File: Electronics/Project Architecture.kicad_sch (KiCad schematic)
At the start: 5 parts

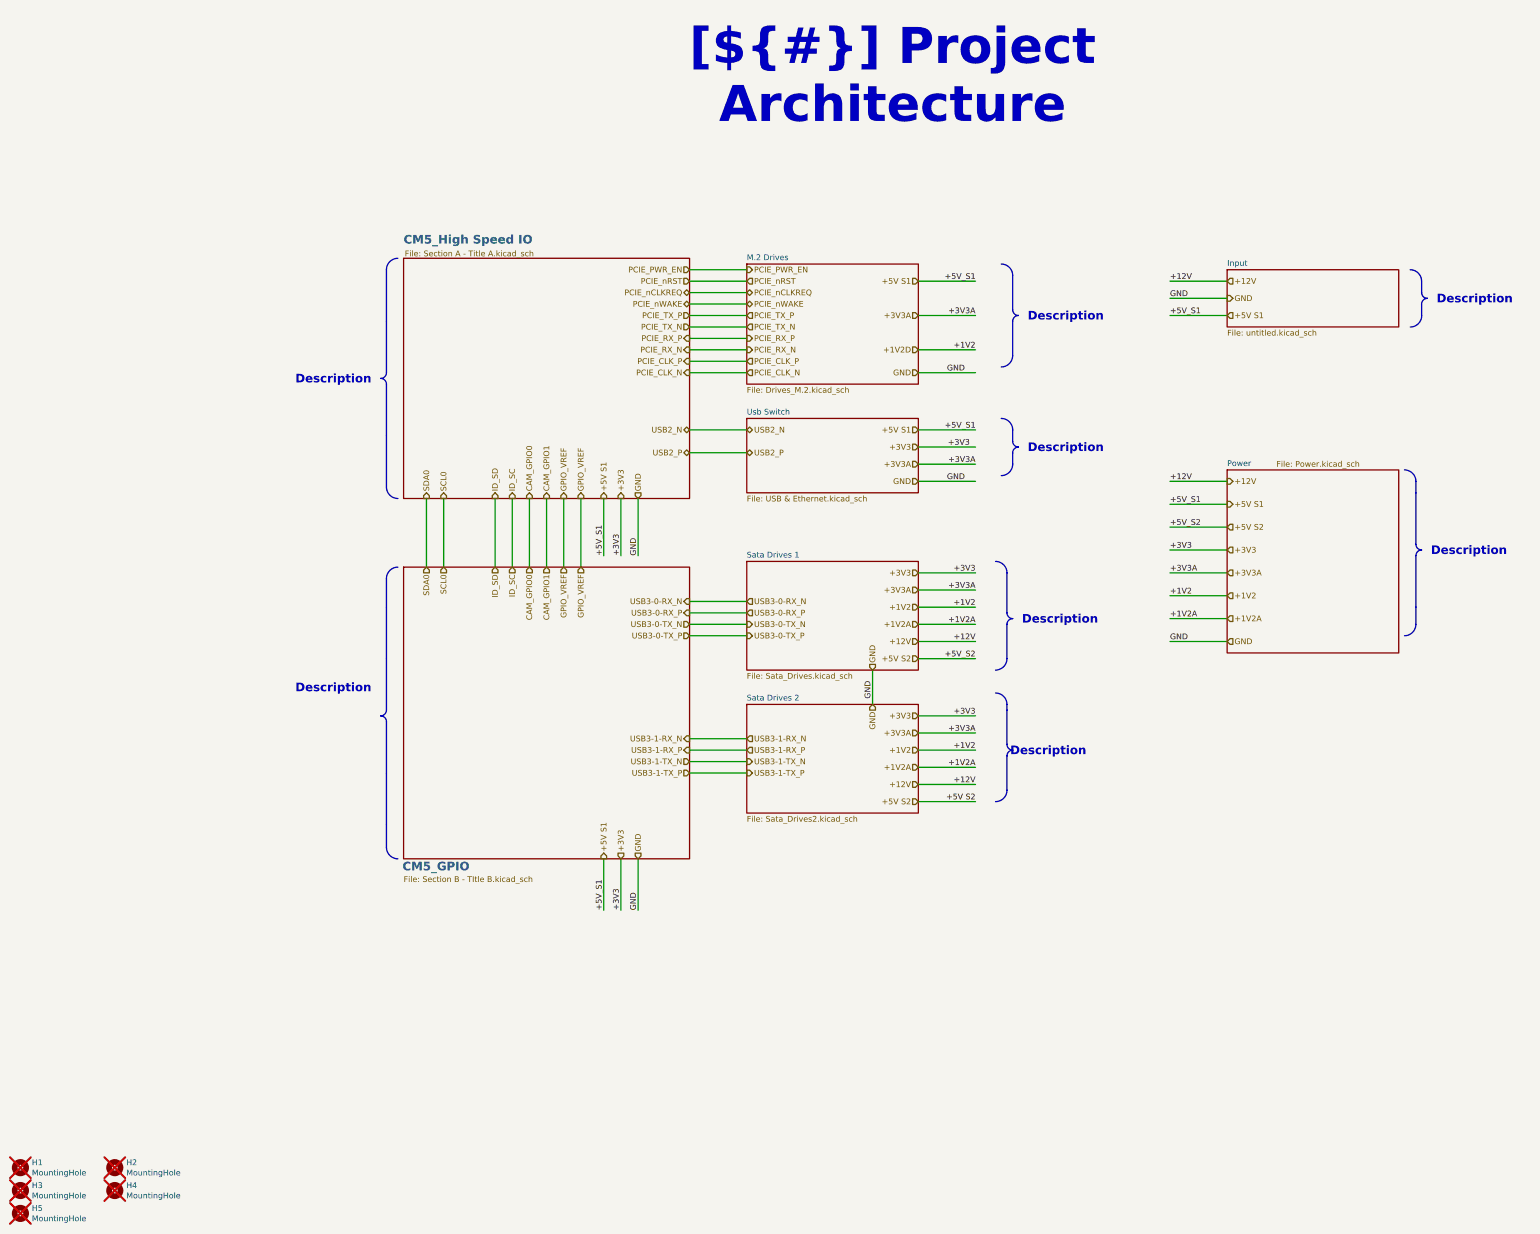
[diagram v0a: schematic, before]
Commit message: Power symbols changed and sata hub fixed schem
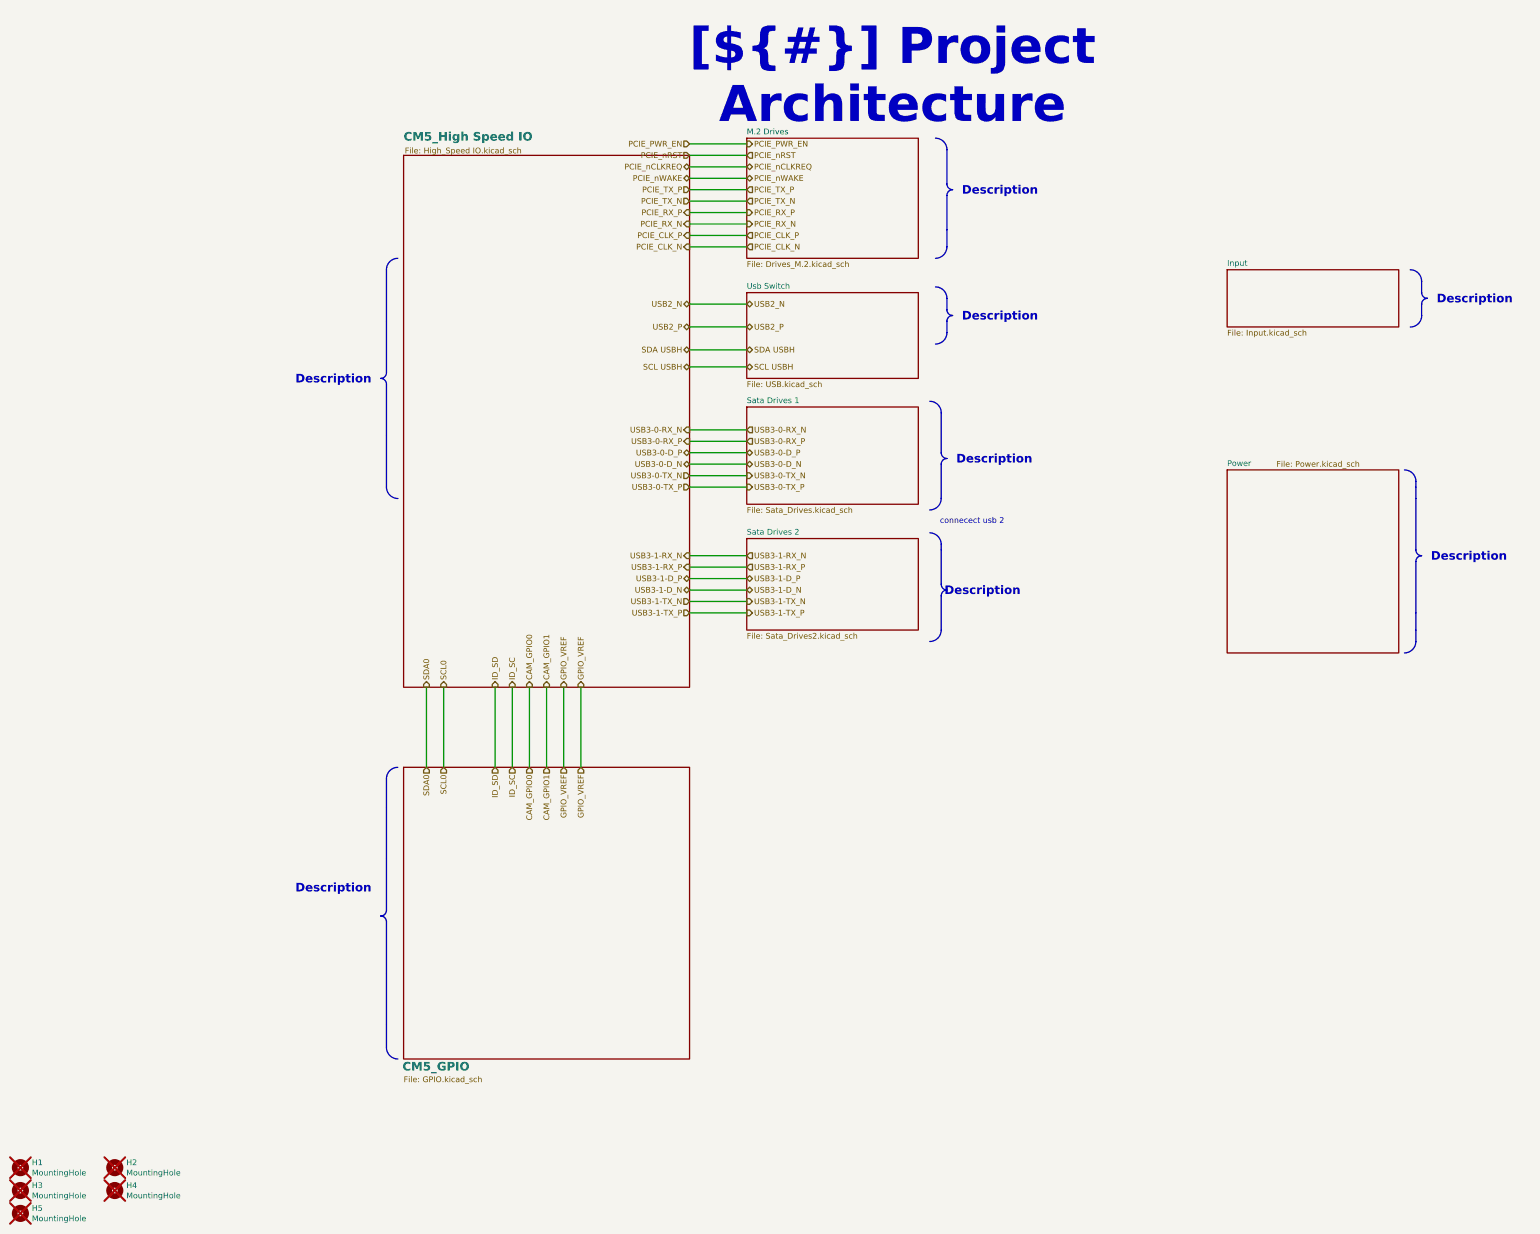
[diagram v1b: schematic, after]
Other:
- sheet CM5_GPIO: file Section B - TItle B.kicad_sch -> GPIO.kicad_sch
- sheet CM5_High Speed IO: file Section A - Title A.kicad_sch -> High_Speed IO.kicad_sch
- sheet Input: file untitled.kicad_sch -> Input.kicad_sch
- sheet Usb Switch: file USB & Ethernet.kicad_sch -> USB.kicad_sch
- note added: "connecect usb 2"
